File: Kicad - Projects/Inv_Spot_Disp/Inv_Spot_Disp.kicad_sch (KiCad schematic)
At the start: 39 parts, among them J1 PWM_Out, J2 Power_Supply, J3 Current_Sense, J6 Rail_Sense, SW1 SW_MEC_5E, SW2 SW_MEC_5E, SW3 SW_MEC_5E, SW4 SW_MEC_5E, SW5 SW_Push, U1 STM32F030F4Px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

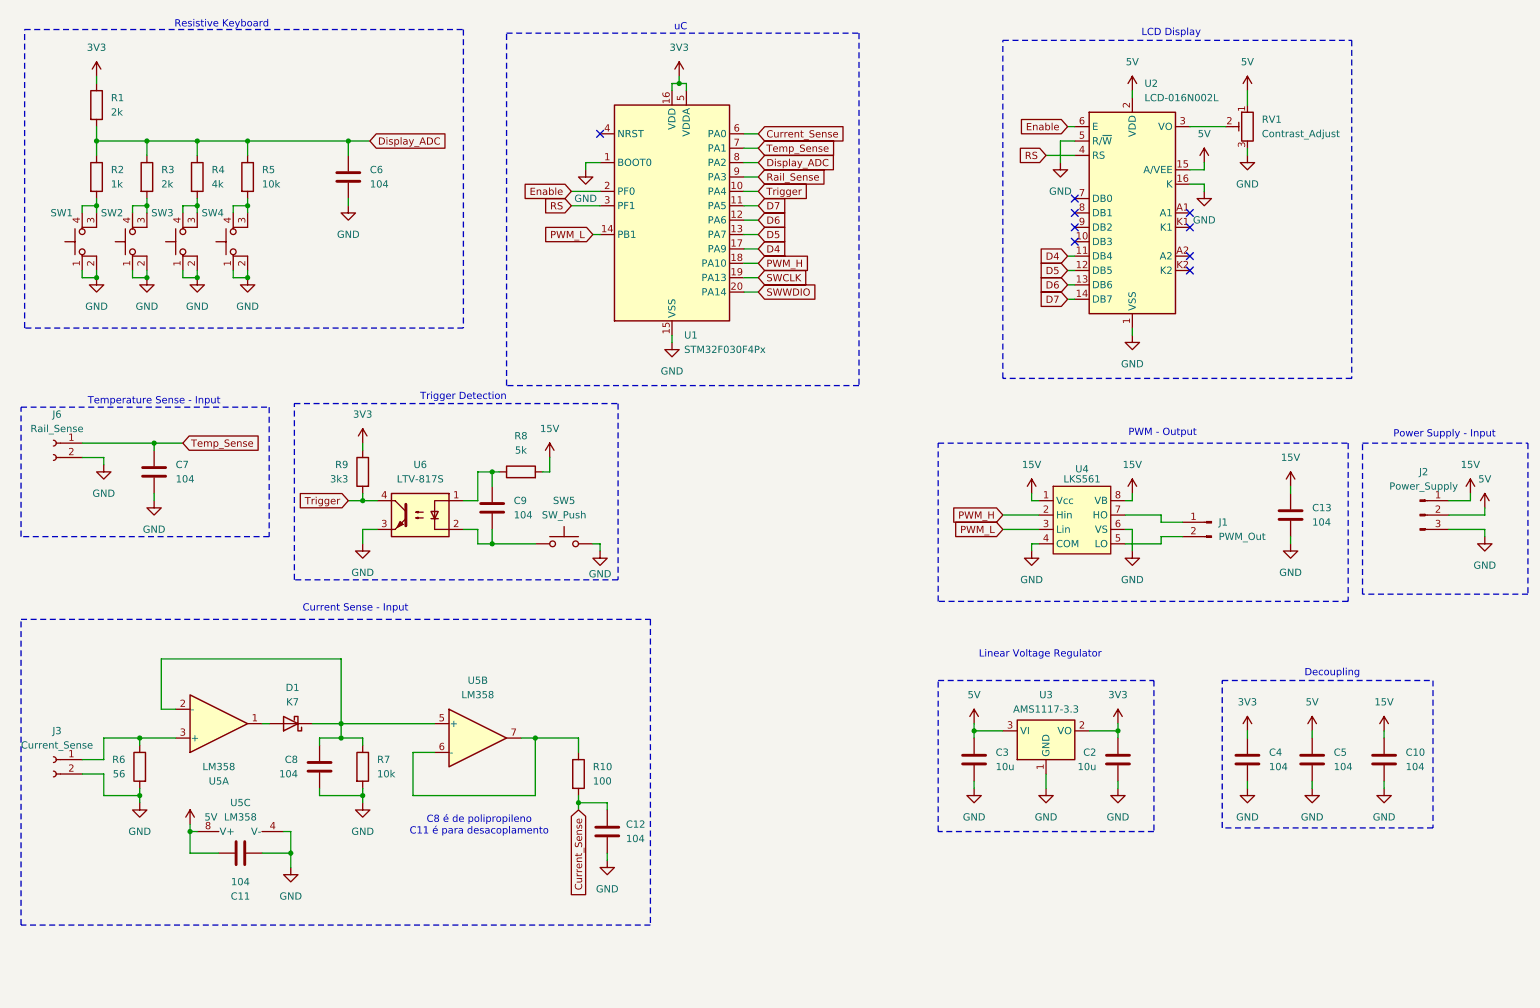
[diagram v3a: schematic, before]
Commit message: Ajustado Pinout - uC
Feito:
 - Adicionado capacitor de bootstrap no driver
 - Ajustado pinout do uC, código gerador de PWM teve que ser alterado para manter ação de gate simétrica
 - Enrolado secundário do transformador
 - Discutido com Anderson sobre esquemáticos e layouts

À fazer:
 - Rotear PCB
 - Corrigir footprints do teclado resistivo
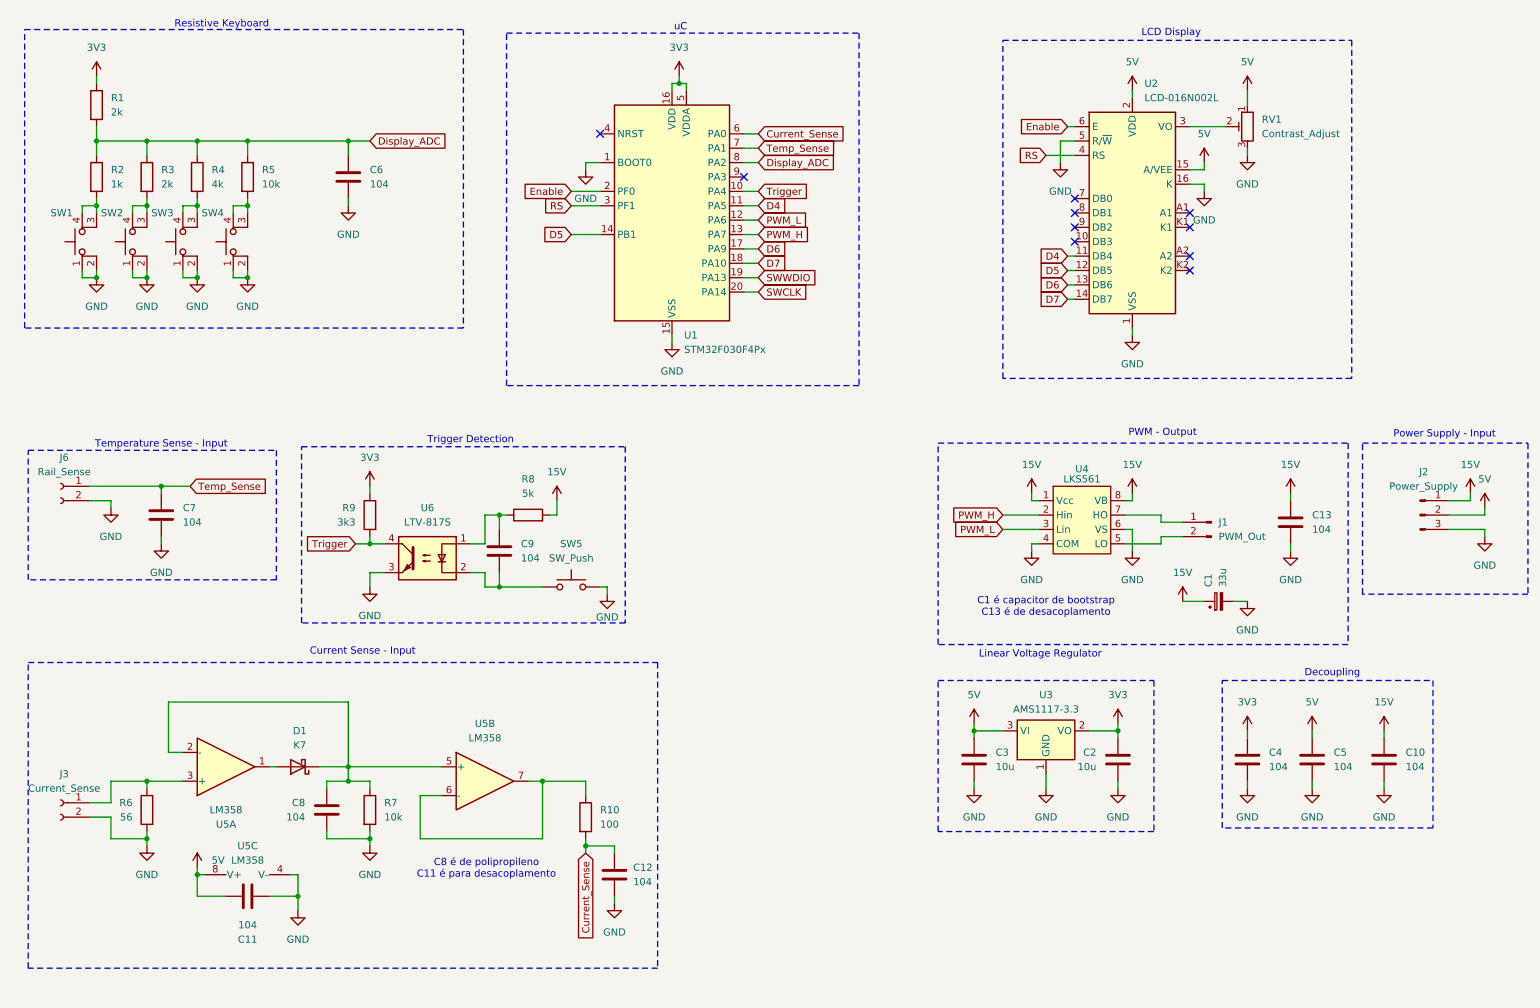
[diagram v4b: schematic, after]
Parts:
- added C1: 33u, Capacitor_THT:CP_Radial_D10.0mm_P5.00mm, symbol Device:C_Polarized_Small
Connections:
- net 15V: now also C1.1
- net D4: now also U1.11 (PA5); no longer U1.17 (PA9)
- net D5: now also U1.14 (PB1); no longer U1.13 (PA7)
- net D6: now also U1.17 (PA9); no longer U1.12 (PA6)
- net D7: now also U1.18 (PA10); no longer U1.11 (PA5)
- net GND: now also C1.2
- net PWM_H: now also U1.13 (PA7); no longer U1.18 (PA10)
- net PWM_L: now also U1.12 (PA6); no longer U1.14 (PB1)
- net SWCLK: now also U1.20 (PA14); no longer U1.19 (PA13)
- net SWWDIO: now also U1.19 (PA13); no longer U1.20 (PA14)
- net Rail_Sense: no longer names the net of U1.9 (PA3)
- no-connect marks 9 -> 10
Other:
- note added: "C1 é capacitor de bootstrap C13 é de desacoplamento"
- moved on the sheet: C11, C12, C13, C7, C8, C9, D1, J3, J6, R10, R6, R7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

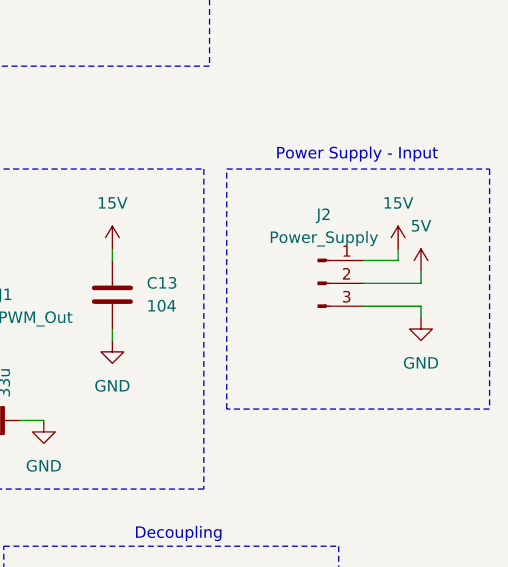
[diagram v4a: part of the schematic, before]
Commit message: Ajuste da Entrada
Ajuste da entrada da fonte auxiliar
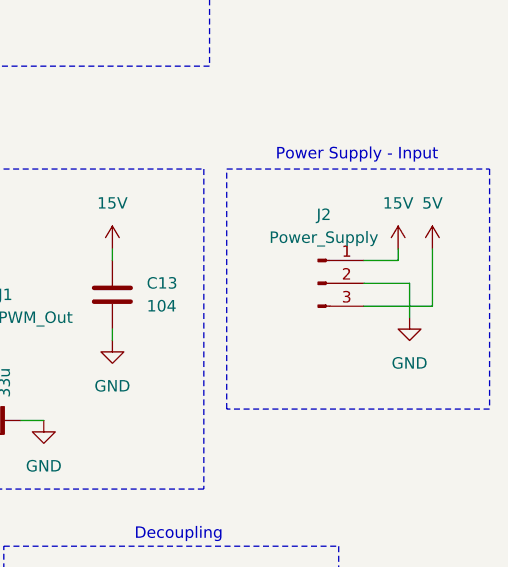
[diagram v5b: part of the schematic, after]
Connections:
- net 5V: now also J2.3 (Pin_3); no longer J2.2 (Pin_2)
- net GND: now also J2.2 (Pin_2); no longer J2.3 (Pin_3)
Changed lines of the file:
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@@
 	(wire
 		(pts
+			(xy 267.97 107.95) (xy 275.59 107.95)
+		)
+		(stroke
+			(width 0)
+			(type default)
+		)
+	)
+	(wire
+		(pts
 			(xy 256.54 152.4) (xy 256.54 153.67)
 		)
@@
 	(wire
 		(pts
+			(xy 267.97 105.41) (xy 273.05 105.41)
+		)
+		(stroke
+			(width 0)
+			(type default)
+		)
+	)
+	(wire
+		(pts
 			(xy 240.03 101.6) (xy 240.03 102.87)
 		)
@@
 	(wire
 		(pts
-			(xy 26.67 62.23) (xy 26.67 63.5)
+			(xy 275.59 107.95) (xy 275.59 101.6)
 		)
 		(stroke
@@
 	(wire
 		(pts
-			(xy 53.34 50.8) (xy 55.88 50.8)
+			(xy 26.67 62.23) (xy 26.67 63.5)
 		)
 		(stroke
@@
 	(wire
 		(pts
-			(xy 59.69 149.86) (xy 60.96 149.86)
+			(xy 53.34 50.8) (xy 55.88 50.8)
 		)
 		(stroke
@@
 	(wire
 		(pts
-			(xy 86.36 154.94) (xy 86.36 162.56)
+			(xy 59.69 149.86) (xy 60.96 149.86)
 		)
 		(stroke
@@
 	(wire
 		(pts
-			(xy 243.84 143.51) (xy 243.84 144.78)
+			(xy 86.36 154.94) (xy 86.36 162.56)
 		)
 		(stroke
@@
 	(wire
 		(pts
-			(xy 46.99 49.53) (xy 46.99 50.8)
+			(xy 243.84 143.51) (xy 243.84 144.78)
 		)
 		(stroke
@@
 	(wire
 		(pts
-			(xy 256.54 143.51) (xy 256.54 144.78)
+			(xy 46.99 49.53) (xy 46.99 50.8)
 		)
 		(stroke
@@
 	(wire
 		(pts
-			(xy 184.15 142.24) (xy 184.15 143.51)
+			(xy 256.54 143.51) (xy 256.54 144.78)
 		)
 		(stroke
@@
 	(wire
 		(pts
-			(xy 267.97 107.95) (xy 274.32 107.95)
+			(xy 184.15 142.24) (xy 184.15 143.51)
 		)
 		(stroke
@@
 	(wire
 		(pts
-			(xy 267.97 105.41) (xy 274.32 105.41)
-		)
-		(stroke
-			(width 0)
-			(type default)
-		)
-	)
-	(wire
-		(pts
 			(xy 46.99 172.72) (xy 46.99 168.91)
 		)
@@
 	(wire
 		(pts
-			(xy 274.32 105.41) (xy 274.32 104.14)
-		)
-		(stroke
-			(width 0)
-			(type default)
-		)
-	)
-	(wire
-		(pts
 			(xy 38.1 39.37) (xy 29.21 39.37)
 		)
@@
 	(wire
 		(pts
-			(xy 274.32 107.95) (xy 274.32 109.22)
+			(xy 273.05 105.41) (xy 273.05 109.22)
 		)
 		(stroke
@@
 	(symbol
 		(lib_id "power:GND")
-		(at 274.32 109.22 0)
+		(at 273.05 109.22 0)
 		(unit 1)
 		(body_style 1)
@@
 		(fields_autoplaced yes)
 		(property "Reference" "#PWR019"
-			(at 274.32 115.57 0)
+			(at 273.05 115.57 0)
 			(hide yes)
 			(show_name no)
@@
 		)
 		(property "Value" "GND"
-			(at 274.32 114.3 0)
+			(at 273.05 114.3 0)
 			(show_name no)
 			(do_not_autoplace no)
@@
 		)
 		(property "Footprint" ""
-			(at 274.32 109.22 0)
+			(at 273.05 109.22 0)
 			(hide yes)
 			(show_name no)
@@
 		)
 		(property "Datasheet" ""
-			(at 274.32 109.22 0)
+			(at 273.05 109.22 0)
 			(hide yes)
 			(show_name no)
@@
 		)
 		(property "Description" "Power symbol creates a global label with name \"GND\" , ground"
-			(at 274.32 109.22 0)
+			(at 273.05 109.22 0)
 			(hide yes)
 			(show_name no)
@@
 	(symbol
 		(lib_id "power:VCC")
-		(at 274.32 104.14 0)
+		(at 275.59 101.6 0)
 		(unit 1)
 		(body_style 1)
@@
 		(fields_autoplaced yes)
 		(property "Reference" "#PWR018"
-			(at 274.32 107.95 0)
+			(at 275.59 105.41 0)
 			(hide yes)
 			(show_name no)
@@
 		)
 		(property "Value" "5V"
-			(at 274.32 99.06 0)
+			(at 275.59 96.52 0)
 			(show_name no)
 			(do_not_autoplace no)
@@
 		)
 		(property "Footprint" ""
-			(at 274.32 104.14 0)
+			(at 275.59 101.6 0)
 			(hide yes)
 			(show_name no)
@@
 		)
 		(property "Datasheet" ""
-			(at 274.32 104.14 0)
+			(at 275.59 101.6 0)
 			(hide yes)
 			(show_name no)
@@
 		)
 		(property "Description" "Power symbol creates a global label with name \"VCC\""
-			(at 274.32 104.14 0)
+			(at 275.59 101.6 0)
 			(hide yes)
 			(show_name no)

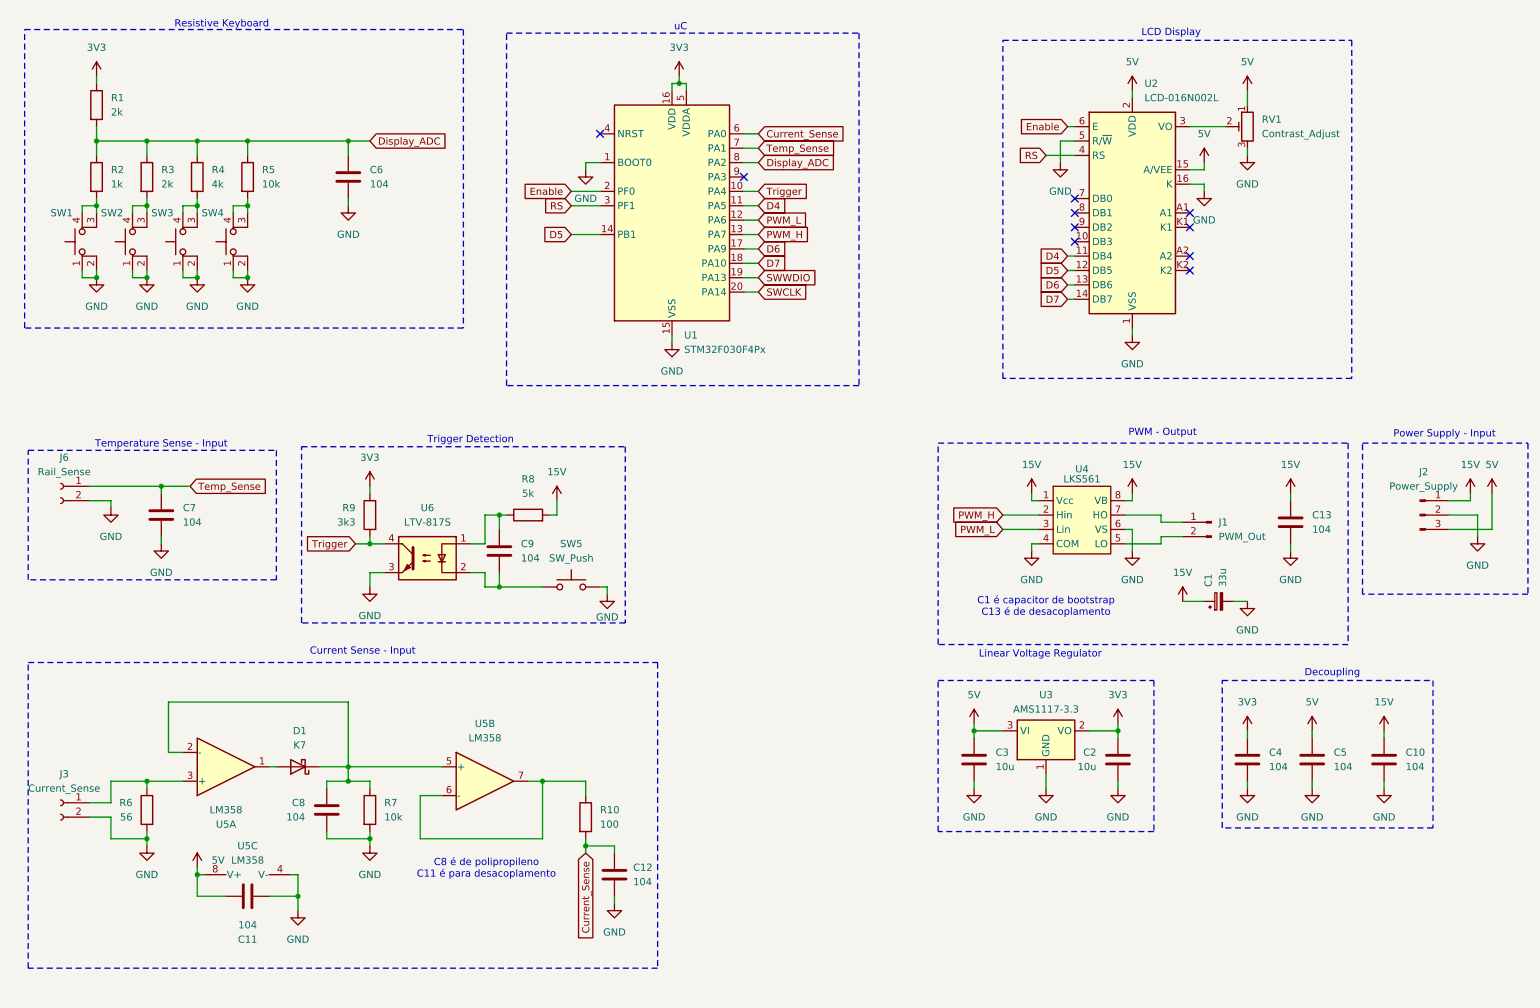
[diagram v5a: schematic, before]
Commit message: Geração de Código
Gerado o código para a nova geração de PWM

Adicionados elementos na PCB

Footprints corrigidos
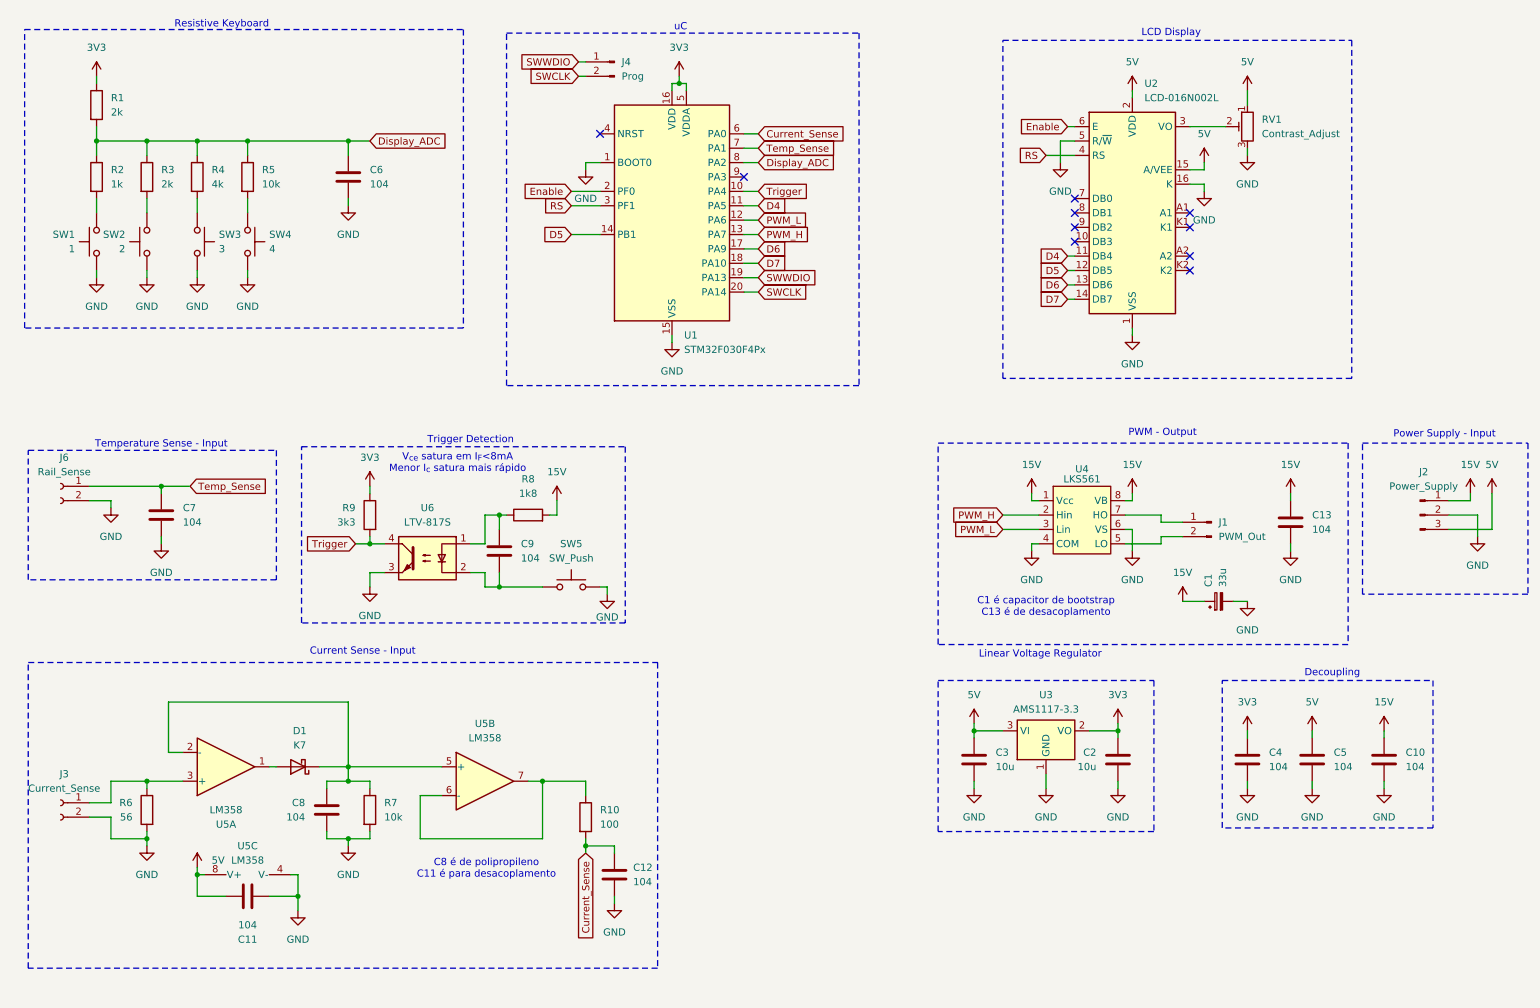
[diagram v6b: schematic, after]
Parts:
- removed SW1, SW2, SW3, SW4: SW_MEC_5E, Button_Switch_THT:Tactile_Switch_W6mm, symbol Switch:SW_MEC_5E
- added J4: Prog, Connector_PinHeader_2.00mm:PinHeader_1x02_P2.00mm_Vertical, symbol Connector:Conn_01x02_Pin
- added SW1: 1, Button_Switch_THT:SW_PUSH_6mm_H13mm, symbol Switch:SW_Push
- added SW2: 2, Button_Switch_THT:SW_PUSH_6mm_H13mm, symbol Switch:SW_Push
- added SW3: 3, Button_Switch_THT:SW_PUSH_6mm_H13mm, symbol Switch:SW_Push
- added SW4: 4, Button_Switch_THT:SW_PUSH_6mm_H13mm, symbol Switch:SW_Push
- R8: value 5k -> 1k8
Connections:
- net GND: now also SW1.1, SW2.1, SW3.1, SW4.1
- net SWCLK: now also J4.2 (Pin_2)
- net SWWDIO: now also J4.1 (Pin_1)
- net at R5.2: now also SW4.2
- net at R2.2: now also SW1.2
- net at R3.2: now also SW2.2
- net at R4.2: now also SW3.2
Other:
- note added: "V_{ce} satura em I_{F}<8mA Menor I_{c} satura mais rápido"
